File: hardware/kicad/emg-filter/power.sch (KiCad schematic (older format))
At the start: 91 parts, among them U2 LM7805_TO220, U3 LM7905_TO220

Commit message: Connector
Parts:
- added J?: Conn_01x03, symbol Connector_Generic:Conn_01x03
- added J?: Conn_01x02, symbol Connector_Generic:Conn_01x02
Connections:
- wire segments 325 -> 336
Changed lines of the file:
@@
 $EndDescr
 Wire Wire Line
-	3300 2350 4300 2350
+	3300 2350 4100 2350
 Connection ~ 7900 3250
 Connection ~ 7900 2050
@@
 Connection ~ 3300 2800
 Wire Wire Line
-	3300 2950 4300 2950
+	3300 2950 4100 2950
 $Comp
 L power:GNDREF #PWR04
@@
 	1    0    0    -1
 $EndComp
+$Comp
+L Connector_Generic:Conn_01x03 J?
+U 1 1 61E44218
+P 3800 2650
+F 0 "J?" H 3800 2450 50  0000 C CNN
+F 1 "Conn_01x03" H 3800 2850 50  0000 C CNN
+F 2 "" H 3800 2650 50  0001 C CNN
+F 3 "~" H 3800 2650 50  0001 C CNN
+	1    3800 2650
+	-1   0    0    1
+$EndComp
+Wire Wire Line
+	4000 2550 4100 2550
+Wire Wire Line
+	4100 2550 4100 2350
+Connection ~ 4100 2350
+Wire Wire Line
+	4100 2350 4300 2350
+Wire Wire Line
+	4000 2750 4100 2750
+Wire Wire Line
+	4100 2750 4100 2950
+Connection ~ 4100 2950
+Wire Wire Line
+	4100 2950 4300 2950
+Wire Wire Line
+	4000 2650 4300 2650
+$Comp
+L Connector_Generic:Conn_01x02 J?
+U 1 1 61EA6DDC
+P 850 2700
+F 0 "J?" H 768 2375 50  0000 C CNN
+F 1 "Conn_01x02" H 768 2466 50  0000 C CNN
+F 2 "" H 850 2700 50  0001 C CNN
+F 3 "~" H 850 2700 50  0001 C CNN
+	1    850  2700
+	-1   0    0    1
+$EndComp
+Wire Wire Line
+	1050 2600 1300 2600
+Wire Wire Line
+	1300 2600 1300 2500
+Wire Wire Line
+	1050 2700 1300 2700
+Wire Wire Line
+	1300 2700 1300 2800
+$Comp
+L power:+24V #PWR?
+U 1 1 61F0B0C6
+P 1300 2500
+F 0 "#PWR?" H 1300 2350 50  0001 C CNN
+F 1 "+24V" H 1315 2673 50  0000 C CNN
+F 2 "" H 1300 2500 50  0001 C CNN
+F 3 "" H 1300 2500 50  0001 C CNN
+	1    1300 2500
+	1    0    0    -1
+$EndComp
+$Comp
+L power:GNDREF #PWR?
+U 1 1 61F0B5A3
+P 1300 2800
+F 0 "#PWR?" H 1300 2550 50  0001 C CNN
+F 1 "GNDREF" H 1305 2627 50  0000 C CNN
+F 2 "" H 1300 2800 50  0001 C CNN
+F 3 "" H 1300 2800 50  0001 C CNN
+	1    1300 2800
+	1    0    0    -1
+$EndComp

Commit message: minor fixes
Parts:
- removed J?: Conn_01x03, symbol Connector_Generic:Conn_01x03
- removed J?: Conn_01x02, symbol Connector_Generic:Conn_01x02
- added J?: Conn_01x03, symbol Connector_Generic:Conn_01x03
- added J?: Conn_01x02, symbol Connector_Generic:Conn_01x02
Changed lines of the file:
@@
 	1    0    0    -1
-$EndComp
-$Comp
-L Connector_Generic:Conn_01x03 J?
-U 1 1 61E44218
-P 3800 2650
-F 0 "J?" H 3800 2450 50  0000 C CNN
-F 1 "Conn_01x03" H 3800 2850 50  0000 C CNN
-F 2 "" H 3800 2650 50  0001 C CNN
-F 3 "~" H 3800 2650 50  0001 C CNN
-	1    3800 2650
-	-1   0    0    1
 $EndComp
 Wire Wire Line
@@
 	4000 2650 4300 2650
 $Comp
+L Connector_Generic:Conn_01x03 J?
+U 1 1 61FD4447
+P 3800 2650
+F 0 "J?" H 3800 2450 50  0000 C CNN
+F 1 "Conn_01x03" H 3800 2850 50  0000 C CNN
+F 2 "" H 3800 2650 50  0001 C CNN
+F 3 "~" H 3800 2650 50  0001 C CNN
+	1    3800 2650
+	-1   0    0    -1
+$EndComp
+$Comp
 L Connector_Generic:Conn_01x02 J?
-U 1 1 61EA6DDC
-P 850 2700
-F 0 "J?" H 768 2375 50  0000 C CNN
-F 1 "Conn_01x02" H 768 2466 50  0000 C CNN
-F 2 "" H 850 2700 50  0001 C CNN
-F 3 "~" H 850 2700 50  0001 C CNN
-	1    850  2700
-	-1   0    0    1
+U 1 1 61FD444D
+P 1125 2600
+AR Path="/61C38667/61FD444D" Ref="J?"  Part="1"
+AR Path="/61C389A8/61FD444D" Ref="J?"  Part="1"
+F 0 "J?" H 1043 2275 50  0000 C CNN
+F 1 "Conn_01x02" H 1043 2366 50  0000 C CNN
+F 2 "" H 1125 2600 50  0001 C CNN
+F 3 "~" H 1125 2600 50  0001 C CNN
+	1    1125 2600
+	-1   0    0    -1
 $EndComp
 Wire Wire Line
-	1050 2600 1300 2600
+	1325 2600 1525 2600
 Wire Wire Line
-	1300 2600 1300 2500
+	1325 2700 1525 2700
 Wire Wire Line
-	1050 2700 1300 2700
+	1525 2600 1525 2500
 Wire Wire Line
-	1300 2700 1300 2800
+	1525 2700 1525 2800
 $Comp
 L power:+24V #PWR?
-U 1 1 61F0B0C6
-P 1300 2500
-F 0 "#PWR?" H 1300 2350 50  0001 C CNN
-F 1 "+24V" H 1315 2673 50  0000 C CNN
-F 2 "" H 1300 2500 50  0001 C CNN
-F 3 "" H 1300 2500 50  0001 C CNN
-	1    1300 2500
+U 1 1 61FD4457
+P 1525 2500
+AR Path="/61C38667/61FD4457" Ref="#PWR?"  Part="1"
+AR Path="/61C389A8/61FD4457" Ref="#PWR?"  Part="1"
+F 0 "#PWR?" H 1525 2350 50  0001 C CNN
+F 1 "+24V" H 1540 2673 50  0000 C CNN
+F 2 "" H 1525 2500 50  0001 C CNN
+F 3 "" H 1525 2500 50  0001 C CNN
+	1    1525 2500
 	1    0    0    -1
 $EndComp
 $Comp
 L power:GNDREF #PWR?
-U 1 1 61F0B5A3
-P 1300 2800
-F 0 "#PWR?" H 1300 2550 50  0001 C CNN
-F 1 "GNDREF" H 1305 2627 50  0000 C CNN
-F 2 "" H 1300 2800 50  0001 C CNN
-F 3 "" H 1300 2800 50  0001 C CNN
-	1    1300 2800
+U 1 1 61FD445D
+P 1525 2800
+AR Path="/61C38667/61FD445D" Ref="#PWR?"  Part="1"
+AR Path="/61C389A8/61FD445D" Ref="#PWR?"  Part="1"
+F 0 "#PWR?" H 1525 2550 50  0001 C CNN
+F 1 "GNDREF" H 1530 2627 50  0000 C CNN
+F 2 "" H 1525 2800 50  0001 C CNN
+F 3 "" H 1525 2800 50  0001 C CNN
+	1    1525 2800
 	1    0    0    -1
 $EndComp

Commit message: fixed rect labels
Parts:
- gave numbers to parts that had none: 66
- renumbered C1 to C21, C2 to C26, C3 to C35, C4 to C52, C5 to C53, C8 to C70, C9 to C71, C11 to C72, C12 to C73, C14 to C74, C15 to C75, C17 to C76, C18 to C77, D2 to D1, D3 to D2, D5 to D3, D6 to D4, R4 to R3, R6 to R4, R7 to R5, R9 to R6, R10 to R7, U2 to U1, U3 to U2
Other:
- note added: "-5V caps missing"

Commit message: -5V caps and cap voltages
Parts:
- C21: value 0.1uF -> 0.1uF, 50V
- C26: value 1uF -> 1uF, 50V
- C35: value 0.01uF -> 0.01uF, 50V
- C52, C53: value 1100uF -> 1100uF, 50V
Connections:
- wire segments 336 -> 337
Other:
- note removed: "-5V caps missing"
- moved on the sheet: C11, C12, C15, C16, C19, C20, C24, C25, C29, C3, C30, C33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

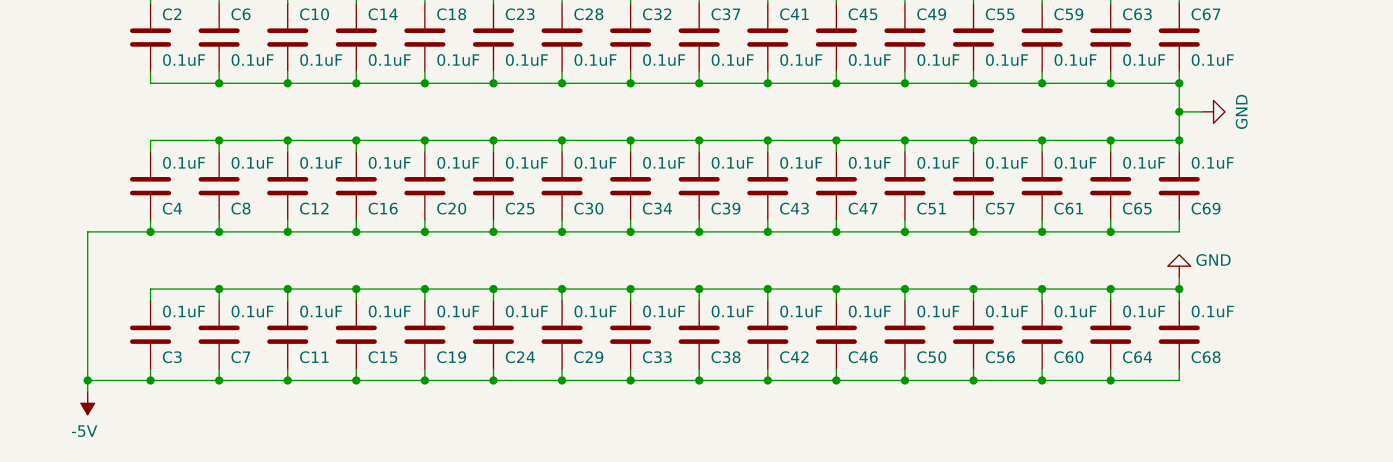
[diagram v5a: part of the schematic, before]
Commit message: footprint association
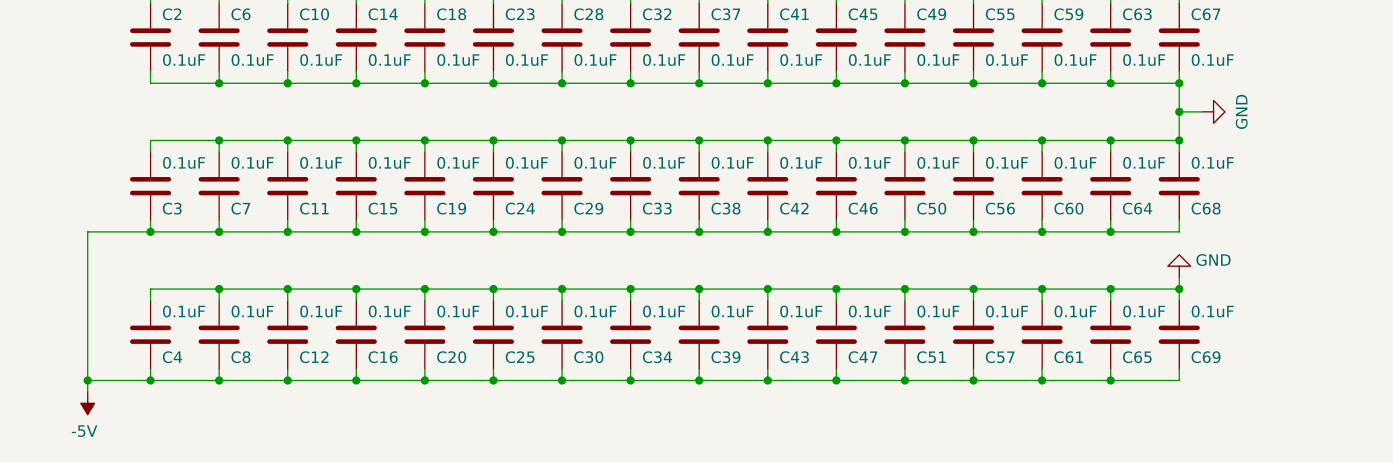
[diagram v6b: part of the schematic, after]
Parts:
- C1, C10, C13, C14, C17, C18, C2, C21, C22, C23, C26, C27, C28, C31, C32, C35, C36, C37, C40, C41, C44, C45, C48, C49, C5, C52, C53, C54, C55, C58, C59, C6, C62, C63, C66, C67, C70, C71, C72, C73, C74, C75, C76, C77, C9: footprint (none) -> Capacitor_SMD:C_0805_2012Metric
- C11: renamed from C12; footprint (none) -> Capacitor_SMD:C_0805_2012Metric
- C12: renamed from C11; footprint (none) -> Capacitor_SMD:C_0805_2012Metric
- C15: renamed from C16; footprint (none) -> Capacitor_SMD:C_0805_2012Metric
- C16: renamed from C15; footprint (none) -> Capacitor_SMD:C_0805_2012Metric
- C19: renamed from C20; footprint (none) -> Capacitor_SMD:C_0805_2012Metric
- C20: renamed from C19; footprint (none) -> Capacitor_SMD:C_0805_2012Metric
- C24: renamed from C25; footprint (none) -> Capacitor_SMD:C_0805_2012Metric
- C25: renamed from C24; footprint (none) -> Capacitor_SMD:C_0805_2012Metric
- C29: renamed from C30; footprint (none) -> Capacitor_SMD:C_0805_2012Metric
- C3: renamed from C4; footprint (none) -> Capacitor_SMD:C_0805_2012Metric
- C30: renamed from C29; footprint (none) -> Capacitor_SMD:C_0805_2012Metric
- C33: renamed from C34; footprint (none) -> Capacitor_SMD:C_0805_2012Metric
- C34: renamed from C33; footprint (none) -> Capacitor_SMD:C_0805_2012Metric
- C38: renamed from C39; footprint (none) -> Capacitor_SMD:C_0805_2012Metric
- C39: renamed from C38; footprint (none) -> Capacitor_SMD:C_0805_2012Metric
- C4: renamed from C3; footprint (none) -> Capacitor_SMD:C_0805_2012Metric
- C42: renamed from C43; footprint (none) -> Capacitor_SMD:C_0805_2012Metric
- C43: renamed from C42; footprint (none) -> Capacitor_SMD:C_0805_2012Metric
- C46: renamed from C47; footprint (none) -> Capacitor_SMD:C_0805_2012Metric
- C47: renamed from C46; footprint (none) -> Capacitor_SMD:C_0805_2012Metric
- C50: renamed from C51; footprint (none) -> Capacitor_SMD:C_0805_2012Metric
- C51: renamed from C50; footprint (none) -> Capacitor_SMD:C_0805_2012Metric
- C56: renamed from C57; footprint (none) -> Capacitor_SMD:C_0805_2012Metric
- C57: renamed from C56; footprint (none) -> Capacitor_SMD:C_0805_2012Metric
- C60: renamed from C61; footprint (none) -> Capacitor_SMD:C_0805_2012Metric
- C61: renamed from C60; footprint (none) -> Capacitor_SMD:C_0805_2012Metric
- C64: renamed from C65; footprint (none) -> Capacitor_SMD:C_0805_2012Metric
- C65: renamed from C64; footprint (none) -> Capacitor_SMD:C_0805_2012Metric
- C68: renamed from C69; footprint (none) -> Capacitor_SMD:C_0805_2012Metric
- C69: renamed from C68; footprint (none) -> Capacitor_SMD:C_0805_2012Metric
- C7: renamed from C8; footprint (none) -> Capacitor_SMD:C_0805_2012Metric
- C8: renamed from C7; footprint (none) -> Capacitor_SMD:C_0805_2012Metric
- D1, D2: footprint (none) -> Diode_SMD:D_SOD-123F
- D3, D4: footprint (none) -> Diode_SMD:D_0805_2012Metric
- R1, R2, R3, R4, R5, R6, R7: footprint (none) -> Resistor_SMD:R_0805_2012Metric
- RV1: footprint (none) -> Connector_PinHeader_2.54mm:PinHeader_1x03_P2.54mm_Vertical

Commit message: Solving Stuff for Free
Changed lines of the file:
@@
 Connection ~ 7900 2050
 $Comp
-L power:PWR_FLAG #FLG02
-U 1 1 61C44E21
-P 775 1250
-F 0 "#FLG02" H 775 1325 50  0001 C CNN
-F 1 "PWR_FLAG" H 775 1423 50  0000 C CNN
-F 2 "" H 775 1250 50  0001 C CNN
-F 3 "~" H 775 1250 50  0001 C CNN
-	1    775  1250
-	1    0    0    -1
-$EndComp
-$Comp
-L power:+5V #PWR01
-U 1 1 61C44E15
-P 775 800
-F 0 "#PWR01" H 775 650 50  0001 C CNN
-F 1 "+5V" H 790 973 50  0000 C CNN
-F 2 "" H 775 800 50  0001 C CNN
-F 3 "" H 775 800 50  0001 C CNN
-	1    775  800
-	1    0    0    -1
-$EndComp
-$Comp
-L power:PWR_FLAG #FLG01
-U 1 1 61C44E1B
-P 775 800
-F 0 "#FLG01" H 775 875 50  0001 C CNN
-F 1 "PWR_FLAG" H 775 973 50  0000 C CNN
-F 2 "" H 775 800 50  0001 C CNN
-F 3 "~" H 775 800 50  0001 C CNN
-	1    775  800
-	-1   0    0    1
-$EndComp
-$Comp
-L power:+24V #PWR05
+L power:+24V #PWR03
 U 1 1 61C5CCAA
 P 1175 800
-F 0 "#PWR05" H 1175 650 50  0001 C CNN
+F 0 "#PWR03" H 1175 650 50  0001 C CNN
 F 1 "+24V" H 1190 973 50  0000 C CNN
 F 2 "" H 1175 800 50  0001 C CNN
@@
 $EndComp
 $Comp
-L power:PWR_FLAG #FLG03
+L power:PWR_FLAG #FLG01
 U 1 1 61C5DB98
 P 1175 800
-F 0 "#FLG03" H 1175 875 50  0001 C CNN
+F 0 "#FLG01" H 1175 875 50  0001 C CNN
 F 1 "PWR_FLAG" H 1175 973 50  0000 C CNN
 F 2 "" H 1175 800 50  0001 C CNN
@@
 	3300 2950 4100 2950
 $Comp
-L power:GNDREF #PWR011
+L power:GNDREF #PWR09
 U 1 1 61D986E3
 P 1950 2800
-F 0 "#PWR011" H 1950 2550 50  0001 C CNN
+F 0 "#PWR09" H 1950 2550 50  0001 C CNN
 F 1 "GNDREF" H 1955 2627 50  0000 C CNN
 F 2 "" H 1950 2800 50  0001 C CNN
@@
 	8800 2650 8800 2700
 $Comp
-L power:GND #PWR016
+L power:GND #PWR014
 U 1 1 61D1A2AE
 P 8800 2700
-F 0 "#PWR016" H 8800 2450 50  0001 C CNN
+F 0 "#PWR014" H 8800 2450 50  0001 C CNN
 F 1 "GND" H 8805 2527 50  0000 C CNN
 F 2 "" H 8800 2700 50  0001 C CNN
@@
 	7900 2050 8800 2050
 $Comp
-L power:+5V #PWR015
+L power:+5V #PWR013
 U 1 1 61DA16DE
 P 8800 2000
-F 0 "#PWR015" H 8800 1850 50  0001 C CNN
+F 0 "#PWR013" H 8800 1850 50  0001 C CNN
 F 1 "+5V" H 8815 2173 50  0000 C CNN
 F 2 "" H 8800 2000 50  0001 C CNN
@@
 $EndComp
 $Comp
-L power:-5V #PWR017
+L power:-5V #PWR015
 U 1 1 61D9BE69
 P 8800 3300
-F 0 "#PWR017" H 8800 3400 50  0001 C CNN
+F 0 "#PWR015" H 8800 3400 50  0001 C CNN
 F 1 "-5V" H 8815 3473 50  0000 C CNN
 F 2 "" H 8800 3300 50  0001 C CNN
@@
 $EndComp
 $Comp
-L power:GNDREF #PWR09
+L power:GNDREF #PWR07
 U 1 1 61C630D3
 P 1575 1250
-F 0 "#PWR09" H 1575 1000 50  0001 C CNN
+F 0 "#PWR07" H 1575 1000 50  0001 C CNN
 F 1 "GNDREF" H 1580 1077 50  0000 C CNN
 F 2 "" H 1575 1250 50  0001 C CNN
@@
 $EndComp
 $Comp
-L power:PWR_FLAG #FLG05
+L power:PWR_FLAG #FLG03
 U 1 1 61C6230F
 P 1575 1250
-F 0 "#FLG05" H 1575 1325 50  0001 C CNN
+F 0 "#FLG03" H 1575 1325 50  0001 C CNN
 F 1 "PWR_FLAG" H 1575 1423 50  0000 C CNN
 F 2 "" H 1575 1250 50  0001 C CNN
 F 3 "~" H 1575 1250 50  0001 C CNN
 	1    1575 1250
-	1    0    0    -1
-$EndComp
-$Comp
-L power:PWR_FLAG #FLG04
-U 1 1 61C44E33
-P 1175 1250
-F 0 "#FLG04" H 1175 1325 50  0001 C CNN
-F 1 "PWR_FLAG" H 1175 1423 50  0000 C CNN
-F 2 "" H 1175 1250 50  0001 C CNN
-F 3 "~" H 1175 1250 50  0001 C CNN
-	1    1175 1250
-	1    0    0    -1
-$EndComp
-$Comp
-L power:GND #PWR06
-U 1 1 61C44E2D
-P 1175 1250
-F 0 "#PWR06" H 1175 1000 50  0001 C CNN
-F 1 "GND" H 1180 1077 50  0000 C CNN
-F 2 "" H 1175 1250 50  0001 C CNN
-F 3 "" H 1175 1250 50  0001 C CNN
-	1    1175 1250
 	1    0    0    -1
 $EndComp
@@
 	5625 7225 5625 7275
 $Comp
-L power:GND #PWR013
+L power:GND #PWR011
 U 1 1 6216511F
 P 5625 7225
-F 0 "#PWR013" H 5625 6975 50  0001 C CNN
+F 0 "#PWR011" H 5625 6975 50  0001 C CNN
 F 1 "GND" H 5775 7150 50  0000 C CNN
 F 2 "" H 5625 7225 50  0001 C CNN
@@
 $EndComp
 $Comp
-L power:GND #PWR012
+L power:GND #PWR010
 U 1 1 6215EAC1
 P 5625 5775
-F 0 "#PWR012" H 5625 5525 50  0001 C CNN
+F 0 "#PWR010" H 5625 5525 50  0001 C CNN
 F 1 "GND" H 5775 5700 50  0000 C CNN
 F 2 "" H 5625 5775 50  0001 C CNN
@@
 	5625 5375 5625 5325
 $Comp
-L power:+5V #PWR03
+L power:+5V #PWR01
 U 1 1 61F8A896
 P 850 5275
-F 0 "#PWR03" H 850 5125 50  0001 C CNN
+F 0 "#PWR01" H 850 5125 50  0001 C CNN
 F 1 "+5V" H 865 5448 50  0000 C CNN
 F 2 "" H 850 5275 50  0001 C CNN
@@
 $EndComp
 $Comp
-L power:+24V #PWR010
+L power:+24V #PWR08
 U 1 1 61C64DCC
 P 1950 2500
-F 0 "#PWR010" H 1950 2350 50  0001 C CNN
+F 0 "#PWR08" H 1950 2350 50  0001 C CNN
 F 1 "+24V" H 1965 2673 50  0000 C CNN
 F 2 "" H 1950 2500 50  0001 C CNN
@@
 $EndComp
 $Comp
-L power:GND #PWR014
+L power:GND #PWR012
 U 1 1 623246A6
 P 5725 6500
-F 0 "#PWR014" H 5725 6250 50  0001 C CNN
+F 0 "#PWR012" H 5725 6250 50  0001 C CNN
 F 1 "GND" H 5725 6325 50  0000 C CNN
 F 2 "" H 5725 6500 50  0001 C CNN
@@
 	1525 2700 1525 2800
 $Comp
-L power:+24V #PWR07
+L power:+24V #PWR05
 U 1 1 61FD4457
 P 1525 2500
-AR Path="/61C38667/61FD4457" Ref="#PWR07"  Part="1"
+AR Path="/61C38667/61FD4457" Ref="#PWR05"  Part="1"
 AR Path="/61C389A8/61FD4457" Ref="#PWR?"  Part="1"
-F 0 "#PWR07" H 1525 2350 50  0001 C CNN
+F 0 "#PWR05" H 1525 2350 50  0001 C CNN
 F 1 "+24V" H 1540 2673 50  0000 C CNN
 F 2 "" H 1525 2500 50  0001 C CNN
@@
 $EndComp
 $Comp
-L power:GNDREF #PWR08
+L power:GNDREF #PWR06
 U 1 1 61FD445D
 P 1525 2800
-AR Path="/61C38667/61FD445D" Ref="#PWR08"  Part="1"
+AR Path="/61C38667/61FD445D" Ref="#PWR06"  Part="1"
 AR Path="/61C389A8/61FD445D" Ref="#PWR?"  Part="1"
-F 0 "#PWR08" H 1525 2550 50  0001 C CNN
+F 0 "#PWR06" H 1525 2550 50  0001 C CNN
 F 1 "GNDREF" H 1530 2627 50  0000 C CNN
 F 2 "" H 1525 2800 50  0001 C CNN
@@
 $Comp
 L power:-5V #PWR02
-U 1 1 61C44E27
-P 775 1250
-F 0 "#PWR02" H 775 1350 50  0001 C CNN
-F 1 "-5V" H 790 1423 50  0000 C CNN
-F 2 "" H 775 1250 50  0001 C CNN
-F 3 "" H 775 1250 50  0001 C CNN
-	1    775  1250
-	-1   0    0    1
-$EndComp
-$Comp
-L power:-5V #PWR04
 U 1 1 6242C6D7
 P 850 7725
-F 0 "#PWR04" H 850 7825 50  0001 C CNN
+F 0 "#PWR02" H 850 7825 50  0001 C CNN
 F 1 "-5V" H 865 7898 50  0000 C CNN
 F 2 "" H 850 7725 50  0001 C CNN
@@
 	1    0    0    -1
 $EndComp
+$Comp
+L power:GND #PWR04
+U 1 1 61C44E2D
+P 1175 1250
+F 0 "#PWR04" H 1175 1000 50  0001 C CNN
+F 1 "GND" H 1180 1077 50  0000 C CNN
+F 2 "" H 1175 1250 50  0001 C CNN
+F 3 "" H 1175 1250 50  0001 C CNN
+	1    1175 1250
+	1    0    0    -1
+$EndComp
+$Comp
+L power:PWR_FLAG #FLG02
+U 1 1 61C44E33
+P 1175 1250
+F 0 "#FLG02" H 1175 1325 50  0001 C CNN
+F 1 "PWR_FLAG" H 1175 1423 50  0000 C CNN
+F 2 "" H 1175 1250 50  0001 C CNN
+F 3 "~" H 1175 1250 50  0001 C CNN
+	1    1175 1250
+	1    0    0    -1
+$EndComp

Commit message: Renaming Labels
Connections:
- wire segments 337 -> 342
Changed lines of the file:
@@
 	8800 2650 8800 2700
 $Comp
-L power:GND #PWR014
+L power:GND #PWR012
 U 1 1 61D1A2AE
 P 8800 2700
-F 0 "#PWR014" H 8800 2450 50  0001 C CNN
+F 0 "#PWR012" H 8800 2450 50  0001 C CNN
 F 1 "GND" H 8805 2527 50  0000 C CNN
 F 2 "" H 8800 2700 50  0001 C CNN
@@
 	7900 2050 8800 2050
 $Comp
-L power:+5V #PWR013
+L power:+5V #PWR011
 U 1 1 61DA16DE
 P 8800 2000
-F 0 "#PWR013" H 8800 1850 50  0001 C CNN
+F 0 "#PWR011" H 8800 1850 50  0001 C CNN
 F 1 "+5V" H 8815 2173 50  0000 C CNN
 F 2 "" H 8800 2000 50  0001 C CNN
@@
 $EndComp
 $Comp
-L power:-5V #PWR015
+L power:-5V #PWR013
 U 1 1 61D9BE69
 P 8800 3300
-F 0 "#PWR015" H 8800 3400 50  0001 C CNN
+F 0 "#PWR013" H 8800 3400 50  0001 C CNN
 F 1 "-5V" H 8815 3473 50  0000 C CNN
 F 2 "" H 8800 3300 50  0001 C CNN
@@
 Wire Wire Line
 	1125 6975 1125 7025
-Connection ~ 5625 6625
 Wire Wire Line
 	5625 6675 5625 6625
@@
 	1    0    0    1
 $EndComp
-Connection ~ 1125 5975
-Wire Wire Line
-	850  5975 1125 5975
 Connection ~ 1125 5325
 Wire Wire Line
@@
 Wire Wire Line
 	1125 5375 1125 5325
-Connection ~ 5625 5725
-Wire Wire Line
-	5625 5775 5625 5725
-Connection ~ 5625 6375
-Connection ~ 5625 7275
-Wire Wire Line
-	5625 7225 5625 7275
-$Comp
-L power:GND #PWR011
+$Comp
+L power:GND #PWR010
 U 1 1 6216511F
-P 5625 7225
-F 0 "#PWR011" H 5625 6975 50  0001 C CNN
-F 1 "GND" H 5775 7150 50  0000 C CNN
-F 2 "" H 5625 7225 50  0001 C CNN
-F 3 "" H 5625 7225 50  0001 C CNN
-	1    5625 7225
-	1    0    0    1
-$EndComp
-$Comp
-L power:GND #PWR010
-U 1 1 6215EAC1
-P 5625 5775
-F 0 "#PWR010" H 5625 5525 50  0001 C CNN
-F 1 "GND" H 5775 5700 50  0000 C CNN
-F 2 "" H 5625 5775 50  0001 C CNN
-F 3 "" H 5625 5775 50  0001 C CNN
-	1    5625 5775
-	1    0    0    -1
+P 6225 6375
+F 0 "#PWR010" H 6225 6125 50  0001 C CNN
+F 1 "GND" H 6375 6300 50  0000 C CNN
+F 2 "" H 6225 6375 50  0001 C CNN
+F 3 "" H 6225 6375 50  0001 C CNN
+	1    6225 6375
+	-1   0    0    -1
 $EndComp
 Wire Wire Line
@@
 Wire Wire Line
 	5325 5725 5025 5725
-Wire Wire Line
-	850  5975 850  5325
 Connection ~ 850  5325
 Wire Wire Line
@@
 	1    1950 2500
 	1    0    0    -1
-$EndComp
-$Comp
-L power:GND #PWR012
-U 1 1 623246A6
-P 5725 6500
-F 0 "#PWR012" H 5725 6250 50  0001 C CNN
-F 1 "GND" H 5725 6325 50  0000 C CNN
-F 2 "" H 5725 6500 50  0001 C CNN
-F 3 "" H 5725 6500 50  0001 C CNN
-	1    5725 6500
-	0    -1   1    0
 $EndComp
 Wire Wire Line
@@
 $EndComp
 Wire Wire Line
-	5625 6375 5625 6500
-Wire Wire Line
-	5625 6500 5725 6500
-Connection ~ 5625 6500
-Wire Wire Line
-	5625 6500 5625 6625
-Wire Wire Line
-	850  7675 850  7025
-Wire Wire Line
-	850  7025 1125 7025
-Wire Wire Line
 	850  7675 1125 7675
 $Comp
@@
 	1    0    0    1
 $EndComp
-Connection ~ 1125 7025
 Connection ~ 1125 7675
 $Comp
@@
 	1    0    0    -1
 $EndComp
+Wire Wire Line
+	850  6625 1125 6625
+Wire Wire Line
+	850  6625 850  7675
+Connection ~ 1125 6625
+Wire Wire Line
+	1125 6375 850  6375
+Connection ~ 1125 6375
+Wire Wire Line
+	850  5325 850  6375
+Wire Wire Line
+	5625 5725 5625 5850
+Connection ~ 5625 5725
+Connection ~ 5625 5975
+Wire Wire Line
+	5625 7025 5625 7150
+Connection ~ 5625 7025
+Connection ~ 5625 7275
+Wire Wire Line
+	5625 5850 5950 5850
+Wire Wire Line
+	5950 5850 5950 6325
+Wire Wire Line
+	5950 7150 5625 7150
+Connection ~ 5625 5850
+Wire Wire Line
+	5625 5850 5625 5975
+Connection ~ 5625 7150
+Wire Wire Line
+	5625 7150 5625 7275
+Wire Wire Line
+	5950 6325 6225 6325
+Wire Wire Line
+	6225 6325 6225 6375
+Connection ~ 5950 6325
+Wire Wire Line
+	5950 6325 5950 7150
 $EndSCHEMATC
